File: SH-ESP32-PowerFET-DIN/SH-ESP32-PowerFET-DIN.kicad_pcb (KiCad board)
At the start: 4 copper layers, 91.4 x 113.4 mm, 101 parts, among them J101 DBT50G-9.5-4P, J102 DBT50G-9.5-2P, J103 AddressSelect, J105 UPDI, J106 I2C, J107 Switch, J108 Switch, J109 I2C, J110 Switch, J111 Switch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

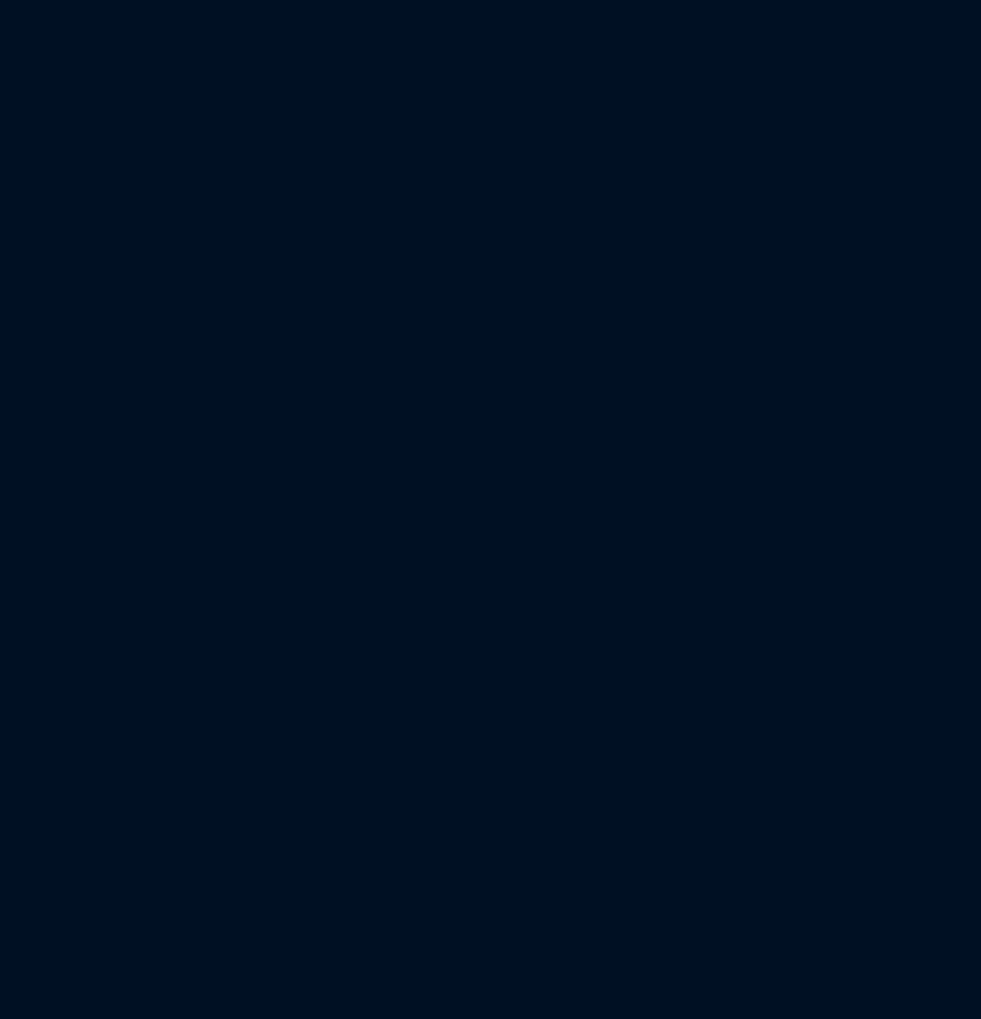
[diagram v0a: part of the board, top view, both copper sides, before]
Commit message: ME MAX 22,5 3-3 layout outlines
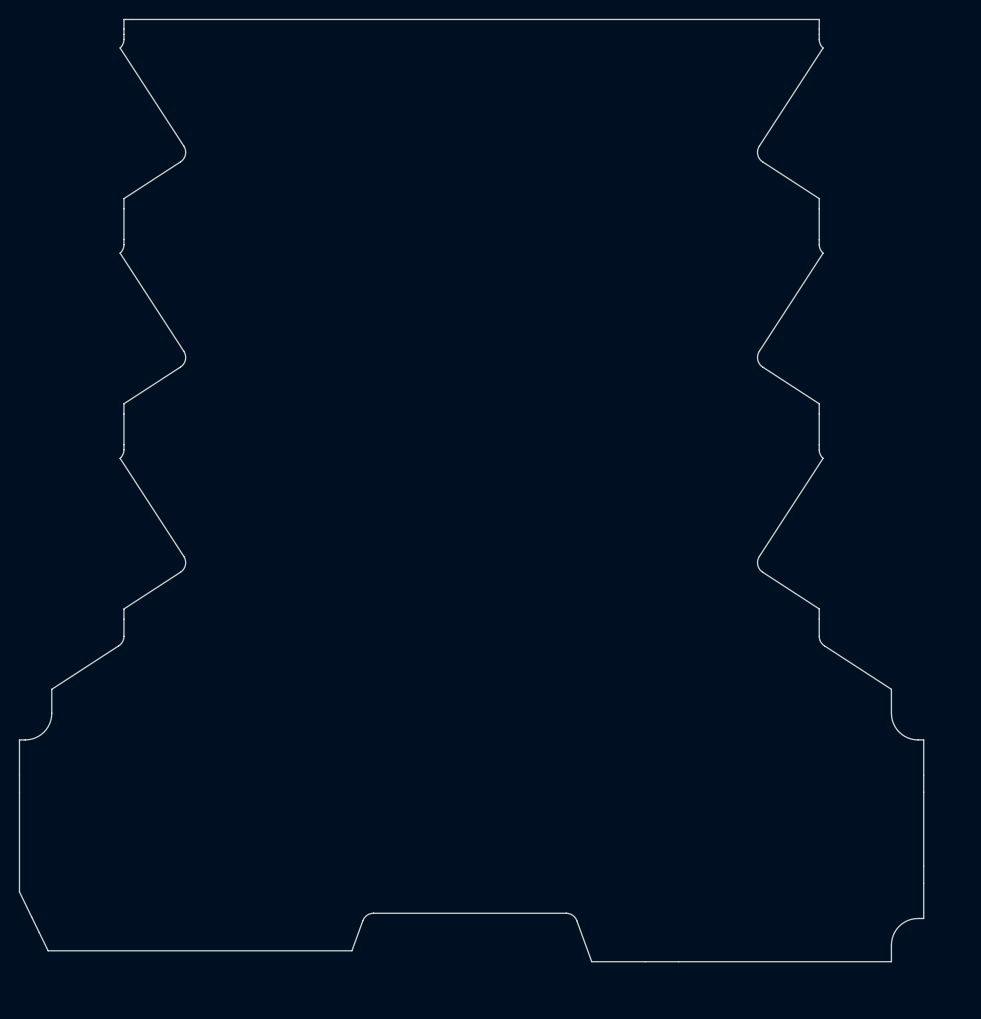
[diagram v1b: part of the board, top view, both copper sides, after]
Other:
- board size 91.4 x 113.4 mm -> 234 x 256.6 mm
